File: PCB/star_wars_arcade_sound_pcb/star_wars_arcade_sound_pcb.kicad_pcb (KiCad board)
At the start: 2 copper layers, 292.1 x 227.3 mm, 15 parts, among them P1 sw_main_connector, P2 sw_aud_connector, P3 sw_audio_edge_connector

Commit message: ICs placed
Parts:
- added A_3: LM556, atari:DIP14, F.Cu at (62.2, 157.5)
- added B_2: TL084, atari:DIP14, F.Cu at (95.2, 138.4)
- added C/D_1: TMS-5220, atari:DIP28, F.Cu at (144.8, 95.9)
- added C_3: TL084, atari:DIP14, F.Cu at (118.1, 158.1)
- added C_4: TL084, atari:DIP14, F.Cu at (118.1, 181.0)
- added F/H_1: 6116, atari:DDIP24, F.Cu at (226.1, 96.5)
- added F/H_5: 74LS125, atari:DIP14, F.Cu at (233.7, 205.7)
- added F_2: C04, atari:DIP14, F.Cu at (222.2, 140.3)
- added F_3: 74LS161, atari:DIP16, F.Cu at (222.2, 164.5)
- added F_5: 74LS161, atari:DIP16, F.Cu at (219.7, 207.0)
- added H_1: 2764, atari:DIP28, F.Cu at (251.5, 99.1)
- added H_2: 74LS04, atari:DIP14, F.Cu at (250.2, 140.3)
- added H_3: 74LS00, atari:DIP14, F.Cu at (250.2, 165.7)
- added H_5: 74LS74, atari:DIP14, F.Cu at (250.2, 205.7)
- moved B_3 209.1 mm to (95.2, 172.7), turned to 180 degrees
- moved K_3 99.0 mm to (288.3, 154.3), turned to 180 degrees
- moved D_2 96.5 mm to (179.1, 139.7), turned to 90 degrees
- moved K_5 91.1 mm to (302.3, 204.5), turned to 180 degrees
- moved P2 81.8 mm to (75.4, 105.9)
- moved D_5 74.1 mm to (179.1, 212.1), turned to 90 degrees
- moved J_5 68.1 mm to (266.7, 204.5), turned to 180 degrees
- moved D_4 50.7 mm to (179.1, 188.0), turned to 90 degrees
- moved E_1 41.9 mm to (195.6, 91.4), turned to 180 degrees
- moved J_3 39.0 mm to (266.7, 164.5), turned to 180 degrees
- moved D_3 38.2 mm to (179.1, 163.8), turned to 90 degrees
- moved J_2 35.0 mm to (266.7, 139.1), turned to 180 degrees
- moved J/K_1 34.0 mm to (274.3, 99.1), turned to 180 degrees

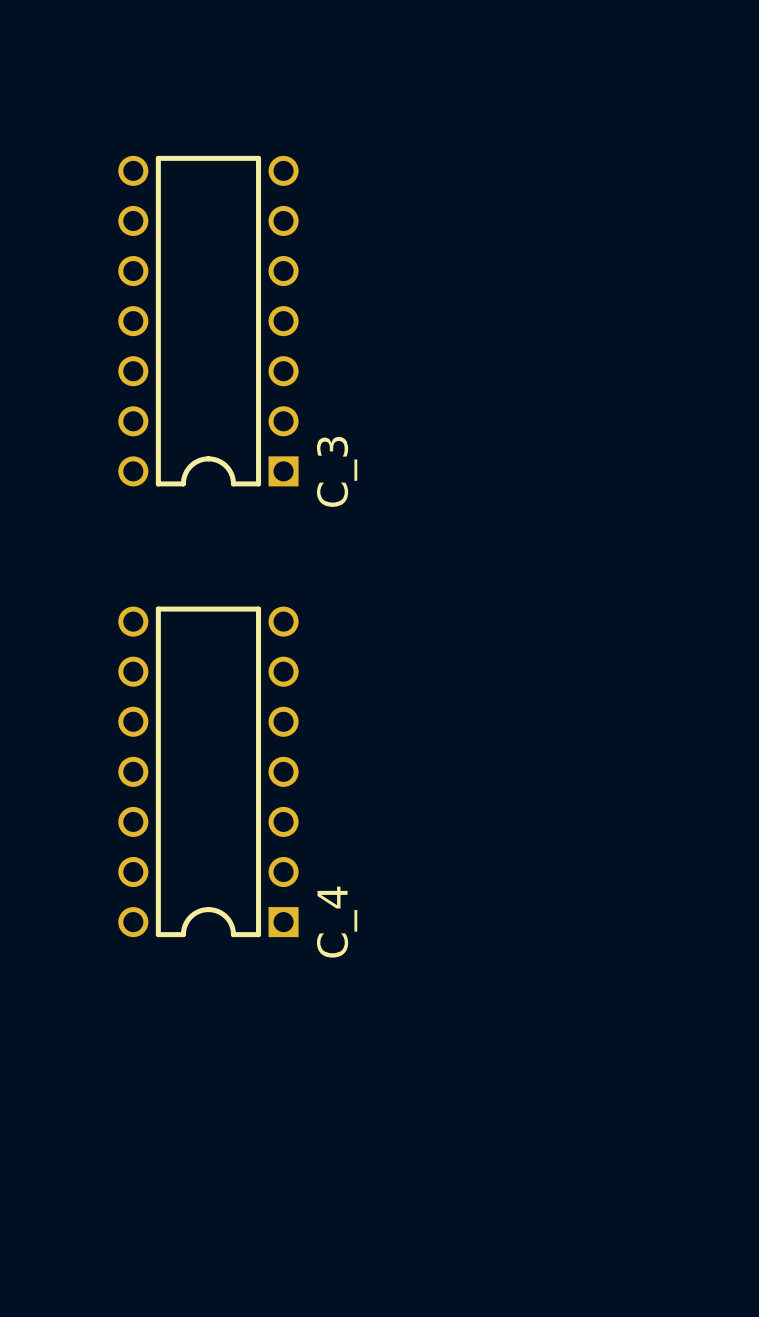
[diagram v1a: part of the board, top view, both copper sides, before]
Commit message: ICs placed
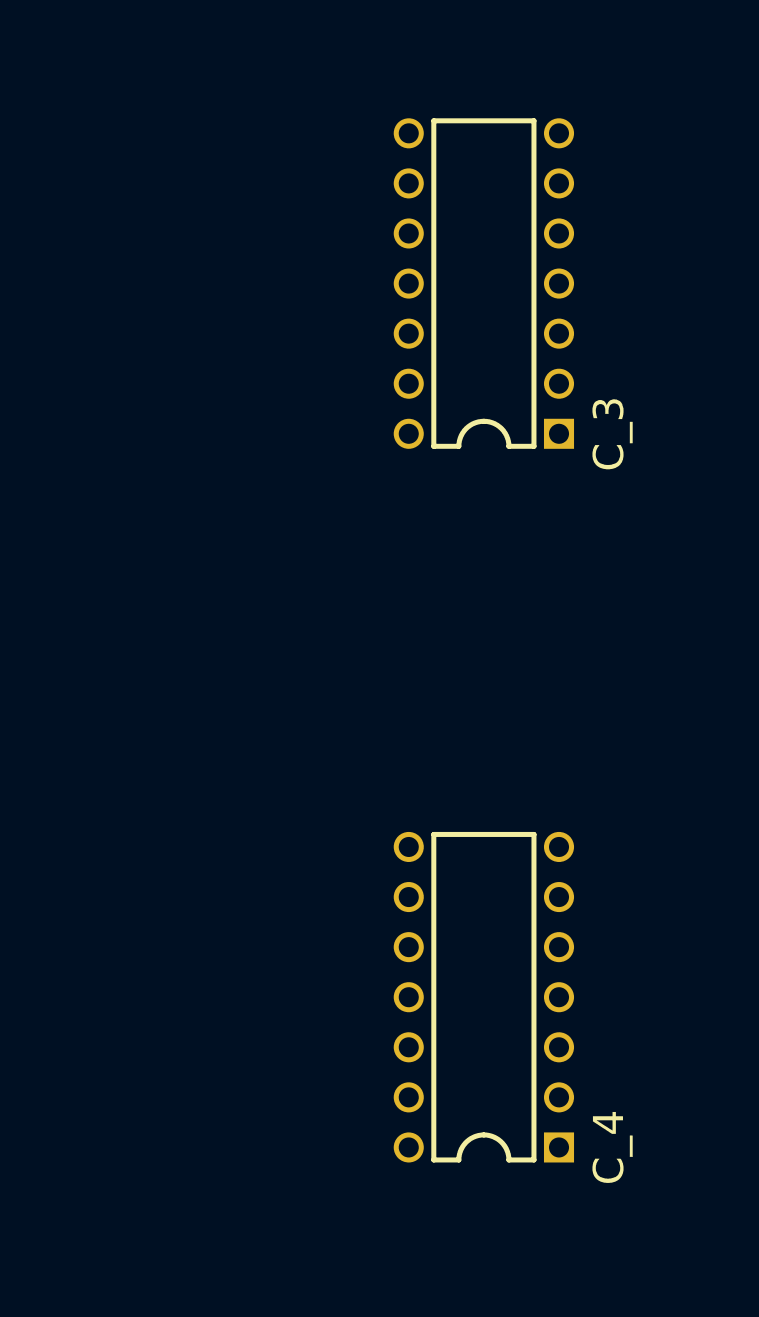
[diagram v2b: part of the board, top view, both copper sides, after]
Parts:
- moved C_4 18.1 mm to (132.1, 192.4)
- moved C_3 14.1 mm to (132.1, 156.2)
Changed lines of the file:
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@@
   )
   (footprint "atari:DIP14" (layer "F.Cu")
-    (at 118.11 158.115 180)
+    (at 132.08 156.21 180)
     (property "Sheetfile" "Sheet16A.kicad_sch")
     (property "Sheetname" "Sheet16A")
@@
   )
   (footprint "atari:DIP14" (layer "F.Cu")
-    (at 118.11 180.975 180)
+    (at 132.08 192.405 180)
     (property "Sheetfile" "Sheet16A.kicad_sch")
     (property "Sheetname" "Sheet16A")

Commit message: Placed all components
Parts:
- added C1: .1uf, atari:GenericComp, F.Cu at (305.4, 160.7)
- added C10: .1uf, atari:GenericComp, F.Cu at (252.1, 151.8)
- added C11: .1uf, atari:GenericComp, F.Cu at (252.1, 177.2)
- added C12: .1uf, atari:GenericComp, F.Cu at (304.2, 219.7)
- added C13: 100uf 50v, atari:LargeCap1, F.Cu at (108.6, 106.7)
- added C14: 100uf 50v, atari:LargeCap2, F.Cu at (117.5, 106.7)
- added C15: 100uf 50v, atari:LargeCap1, F.Cu at (44.5, 95.9)
- added C16: .1uf, atari:GenericComp, F.Cu at (201.3, 223.5)
- added C17: .1uf, atari:GenericComp, F.Cu at (201.3, 199.4)
- added C18: .1uf, atari:GenericComp, F.Cu at (201.3, 175.3)
- added C19: .1uf, atari:GenericComp, F.Cu at (201.3, 151.1)
- added C2: .1uf, atari:GenericComp, F.Cu at (272.4, 120.7)
- added C20: .1uf, atari:GenericComp, F.Cu at (268.6, 177.2)
- added C22: .1uf, atari:GenericComp, F.Cu at (222.2, 177.2)
- added C23: .1uf, atari:GenericComp, F.Cu at (222.9, 151.8)
- added C24: .1uf, atari:GenericComp, F.Cu at (222.2, 128.9)
- added C25: .1uf, atari:GenericComp, F.Cu at (160.0, 110.5)
- added C26: .1uf, atari:GenericComp, F.Cu at (156.2, 110.5)
- added C27: .1uf, atari:GenericComp, F.Cu at (125.7, 114.3)
- added C28: .1uf, atari:GenericComp, F.Cu at (144.8, 200.7)
- added C29: 1000pf, atari:GenericComp, F.Cu at (142.2, 203.2)
- added C3: .1uf, atari:GenericComp, F.Cu at (249.6, 120.7)
- added C30: .1uf, atari:GenericComp, F.Cu at (131.4, 203.8)
- added C31: .1uf, atari:GenericComp, F.Cu at (131.4, 206.4)
- added C32: .1uf, atari:GenericComp, F.Cu at (120.0, 187.3)
- added C33: 1000pf, atari:GenericComp, F.Cu at (143.5, 181.6)
- added C34: .1uf, atari:GenericComp, F.Cu at (120.0, 181.6)
- added C35: 1000pf, atari:GenericComp, F.Cu at (142.2, 167.0)
- added C36: .1uf, atari:GenericComp, F.Cu at (131.4, 167.6)
- added C37: .1uf, atari:GenericComp, F.Cu at (131.4, 170.2)
- added C38: .1uf, atari:GenericComp, F.Cu at (120.0, 179.1)
- added C39: 1000pf, atari:GenericComp, F.Cu at (142.2, 145.4)
- added C4: .1uf, atari:GenericComp, F.Cu at (224.2, 115.6)
- added C40: .1uf, atari:GenericComp, F.Cu at (120.0, 176.5)
- added C41: .1uf, atari:GenericComp, F.Cu at (120.0, 194.9)
- added C42: .1uf, atari:GenericComp, F.Cu at (120.0, 189.9)
- added C43: .1uf, atari:GenericComp, F.Cu at (74.9, 151.1)
- added C44: .01uf, atari:GenericComp, F.Cu at (74.9, 160.0)
- added C45: .1uf, atari:GenericComp, F.Cu at (64.1, 168.9)
- added C46: .0027uf, atari:GenericComp, F.Cu at (48.9, 157.5)
- added C47: 100uf 50v, atari:LargeCap1, F.Cu at (47.0, 141.6)
- added C48: .0027uf, atari:GenericComp, F.Cu at (120.0, 165.1)
- added C49: .0027uf, atari:GenericComp, F.Cu at (120.0, 162.6)
- added C5: .1uf, atari:GenericComp, F.Cu at (198.8, 62.2)
- added C50: .0027uf, atari:GenericComp, F.Cu at (120.0, 157.5)
- added C51: .47uf, atari:MedCap1, F.Cu at (97.2, 163.8)
- added C52: 10uf 35v, atari:MedCap1, F.Cu at (97.2, 158.8)
- added C53: 100uf 50v, atari:LargeCap1, F.Cu at (67.3, 179.7)
- added C54: .1uf, atari:GenericComp, F.Cu at (87.6, 183.5)
- added C55: .1uf, atari:GenericComp, F.Cu at (120.0, 152.4)
- added C56: .0027uf, atari:GenericComp, F.Cu at (108.0, 146.1)
- added C57: .0027uf, atari:GenericComp, F.Cu at (108.0, 143.5)
- added C58: .0027uf, atari:GenericComp, F.Cu at (108.0, 138.4)
- added C59: .1uf, atari:GenericComp, F.Cu at (95.2, 149.9)
- added C6: .1uf, atari:GenericComp, F.Cu at (220.3, 219.7)
- added C60: .1uf, atari:GenericComp, F.Cu at (95.2, 152.4)
- added C61: .1uf, atari:GenericComp, F.Cu at (234.3, 217.2)
- added C7: .1uf, atari:GenericComp, F.Cu at (268.6, 151.8)
- added C8: .1uf, atari:GenericComp, F.Cu at (268.0, 219.7)
- added C9: .1uf, atari:GenericComp, F.Cu at (252.1, 217.2)
- added DS1: BLUE LED, atari:LED, F.Cu at (63.5, 115.6)
- added Q1: 2N3906, atari:GenericTrans, F.Cu at (210.8, 145.4)
- added Q2: 2N3906, atari:GenericTrans, F.Cu at (128.3, 103.5)
- added Q3: 2N3904, atari:GenericTrans, F.Cu at (135.9, 116.8)
- added Q4: 2N3904, atari:GenericTrans, F.Cu at (58.4, 141.0)
- added R1: 1k, atari:GenericComp, F.Cu at (243.2, 214.0)
- added R10: 10k, atari:GenericComp, F.Cu at (214.0, 157.5)
- added R11: 3.3k, atari:GenericComp, F.Cu at (209.6, 156.8)
- added R12: 1k, atari:GenericComp, F.Cu at (213.4, 135.3)
- added R13: 10k, atari:GenericComp, F.Cu at (128.3, 95.2)
- added R14: 3.3k, atari:GenericComp, F.Cu at (125.7, 95.2)
- added R15: 1k, atari:GenericComp, F.Cu at (128.3, 114.3)
- added R16: 3.3k, atari:GenericComp, F.Cu at (130.8, 119.4)
- added R17: 10k, atari:GenericComp, F.Cu at (132.7, 88.9)
- added R18: 1.8k, atari:GenericComp, F.Cu at (156.2, 88.9)
- added R19: 100k, atari:GenericComp, F.Cu at (148.0, 203.8)
- added R2: 10k, atari:GenericComp, F.Cu at (305.4, 173.4)
- added R20: 1k, atari:GenericComp, F.Cu at (139.7, 203.2)
- added R21: 47k, atari:GenericComp, F.Cu at (131.4, 208.9)
- added R22: 1k, atari:GenericComp, F.Cu at (141.0, 181.6)
- added R23: 47k, atari:GenericComp, F.Cu at (133.3, 180.3)
- added R24: 1k, atari:GenericComp, F.Cu at (139.7, 167.0)
- added R25: 82k, atari:GenericComp, F.Cu at (133.3, 177.8)
- added R26: 1k, atari:GenericComp, F.Cu at (139.7, 145.4)
- added R27: 82k, atari:GenericComp, F.Cu at (131.4, 139.7)
- added R28: 100k, atari:GenericComp, F.Cu at (120.0, 192.4)
- added R29: 15k, atari:GenericComp, F.Cu at (120.0, 197.5)
- added R3: 10k, atari:GenericComp, F.Cu at (305.4, 175.9)
- added R30: 12k, atari:GenericComp, F.Cu at (120.0, 184.8)
- added R31: 560k, atari:GenericComp, F.Cu at (74.9, 165.1)
- added R32: 560k, atari:GenericComp, F.Cu at (74.9, 153.7)
- added R33: 4.7k, atari:GenericComp, F.Cu at (48.9, 162.6)
- added R34: 4.7k, atari:GenericComp, F.Cu at (48.9, 160.0)
- added R35: 2.2k, atari:GenericComp, F.Cu at (81.9, 146.1)
- added R36: 15, atari:GenericComp, F.Cu at (66.7, 143.5)
- added R37: 10k, atari:GenericComp, F.Cu at (41.3, 135.3)
- added R38: 470, atari:GenericComp, F.Cu at (52.7, 149.2)
- added R39: 12k, atari:GenericComp, F.Cu at (120.0, 174.0)
- added R4: 1k, atari:GenericComp, F.Cu at (217.2, 223.5)
- added R40: 12k, atari:GenericComp, F.Cu at (120.0, 160.0)
- added R41: 68k, atari:GenericComp, F.Cu at (81.9, 171.4)
- added R42: 12k, atari:GenericComp, F.Cu at (81.9, 174.0)
- added R43: 1.5k, atari:GenericComp, F.Cu at (81.9, 168.9)
- added R44: 100, atari:GenericComp, F.Cu at (97.2, 180.3)
- added R45: 470k, atari:GenericComp, F.Cu at (120.0, 154.9)
- added R46: 12k, atari:GenericComp, F.Cu at (120.0, 149.9)
- added R47: 12k, atari:GenericComp, F.Cu at (108.0, 141.0)
- added R48: 22k, atari:GenericComp, F.Cu at (108.0, 130.8)
- added R49: 22k, atari:GenericComp, F.Cu at (108.0, 133.3)
- added R5: 10k, atari:GenericComp, F.Cu at (207.0, 73.0)
- added R50: 47k, atari:GenericComp, F.Cu at (108.0, 128.3)
- added R51: 2.2k, atari:GenericComp, F.Cu at (99.1, 120.7)
- added R52: 22k, atari:GenericComp, F.Cu at (82.5, 133.3)
- added R53: 22k, atari:GenericComp, F.Cu at (82.5, 138.4)
- added R54: 47k, atari:GenericComp, F.Cu at (82.5, 135.9)
- added R55: 47k, atari:GenericComp, F.Cu at (82.5, 130.8)
- added R56: 2.2k, atari:GenericComp, F.Cu at (90.2, 120.7)
- added R6: 10k, atari:GenericComp, F.Cu at (215.9, 63.5)
- added R7: 1k, atari:GenericComp, F.Cu at (57.1, 108.6)
- added R8: 100, atari:GenericComp, F.Cu at (145.4, 63.5)
- added R9: 100, atari:GenericComp, F.Cu at (145.4, 66.0)
- added TP1: tp_2_pin, atari:TEST_POINT, F.Cu at (308.6, 165.1)
- added TP10: tp_2_pin, atari:TEST_POINT, F.Cu at (80.6, 126.4)
- added TP11: tp_2_pin, atari:TEST_POINT, F.Cu at (220.3, 69.8)
- added TP12: tp_2_pin, atari:TEST_POINT, F.Cu at (308.6, 186.7)
- added TP2: tp_2_pin, atari:TEST_POINT, F.Cu at (308.6, 169.5)
- added TP3: tp_2_pin, atari:TEST_POINT, F.Cu at (45.7, 123.2)
- added TP4: tp_2_pin, atari:TEST_POINT, F.Cu at (59.7, 130.8)
- added TP5: tp_2_pin, atari:TEST_POINT, F.Cu at (57.1, 125.7)
- added TP6: tp_2_pin, atari:TEST_POINT, F.Cu at (54.6, 120.7)
- added TP7: tp_2_pin, atari:TEST_POINT, F.Cu at (212.1, 69.8)
- added TP8: tp_2_pin, atari:TEST_POINT, F.Cu at (104.1, 188.0)
- added TP9: tp_2_pin, atari:TEST_POINT, F.Cu at (108.0, 125.1)
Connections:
- F/H_5 pad 11: (no net) -> unconnected-(F/H_5-Pad11)
- F/H_5 pad 12: (no net) -> GND
- F/H_5 pad 13: (no net) -> GND
- F_2 pad 10: (no net) -> unconnected-(F_2-Pad10)
- F_2 pad 11: (no net) -> GND
- F_2 pad 3: (no net) -> GND
- F_2 pad 4: (no net) -> unconnected-(F_2-Pad4)
- F_2 pad 5: (no net) -> GND
- F_2 pad 6: (no net) -> unconnected-(F_2-Pad6)
- F_2 pad 8: (no net) -> unconnected-(F_2-Pad8)
- F_2 pad 9: (no net) -> GND
- H_2 pad 5: (no net) -> GND
- H_2 pad 6: (no net) -> unconnected-(H_2-Pad6)
- H_2 pad 8: (no net) -> unconnected-(H_2-Pad8)
- H_2 pad 9: (no net) -> GND
- H_3 pad 4: (no net) -> unconnected-(H_3-Pad4)
- H_3 pad 5: (no net) -> unconnected-(H_3-Pad5)
- H_3 pad 6: (no net) -> unconnected-(H_3-Pad6)
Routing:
- net Net-(B_2-Pad6): track 0.00 -> 18.2 mm
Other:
- board text added: "+"

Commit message: Silkscreen work
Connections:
- H_3 pad 10: (no net) -> unconnected-(H_3-Pad10)
- H_3 pad 8: (no net) -> unconnected-(H_3-Pad8)
- H_3 pad 9: (no net) -> unconnected-(H_3-Pad9)
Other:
- board text added: "+12"
- board text added: "+5"
- board text added: "-5"
- board text added: "1"
- board text added: "15"
- board text added: "2"
- board text added: "85"
- board text added: "86"
- board text added: "A"
- board text added: "GND"
- board text added: "S"
- board text added: "SELF TEST"
- board text added: "X07"
- board text added: "X08"

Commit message: Trace work
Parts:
- moved C8 1.42 mm to (266.7, 219.1)
- moved C1 0.63 mm to (306.1, 160.7)
- moved K_3 0.63 mm to (288.9, 154.3)
- moved R2 0.63 mm to (306.1, 173.4)
- moved R3 0.63 mm to (306.1, 175.9)
- moved TP1 0.63 mm to (309.2, 165.1)
- moved TP12 0.63 mm to (309.2, 186.7)
- moved TP2 0.63 mm to (309.2, 169.5)
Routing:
- net +5V: track 0.00 -> 1330.0 mm, vias 0 -> 10
- net +12V: track 0.00 -> 329.2 mm, vias 0 -> 1
- net GND: track 0.00 -> 243.0 mm, vias 0 -> 7
- net SD3: track 0.00 -> 233.3 mm, vias 0 -> 3
- net -5V: track 0.00 -> 229.9 mm, vias 0 -> 1
- net SD1: track 0.00 -> 229.3 mm, vias 0 -> 3
- net SD4: track 0.00 -> 225.0 mm, vias 0 -> 4
- net SD2: track 0.00 -> 223.8 mm, vias 0 -> 3
- net SD0: track 0.00 -> 209.1 mm, vias 0 -> 3
- net PD7: track 0.00 -> 202.7 mm, vias 0 -> 3
- net SD5: track 0.00 -> 198.6 mm, vias 0 -> 3
- net PD6: track 0.00 -> 197.6 mm, vias 0 -> 3
- net PD5: track 0.00 -> 192.5 mm, vias 0 -> 3
- net PD4: track 0.00 -> 187.5 mm, vias 0 -> 3
- net PD3: track 0.00 -> 177.3 mm, vias 0 -> 3
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- added copper zone on B.Cu, net +5V
- added copper zone on F.Cu, net +5V
